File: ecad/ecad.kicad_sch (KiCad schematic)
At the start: 28 parts, among them J1 Raspberry_Pi_2_3, Q1 BC547, Q2 BC547, Q4 BC547, SW1 Power Button, SW2 SW_Push, SW3 SW_Push, U2 USB PD/QC Decoy, U3 VRB1205YMD_6wr3, U6 Power Bank

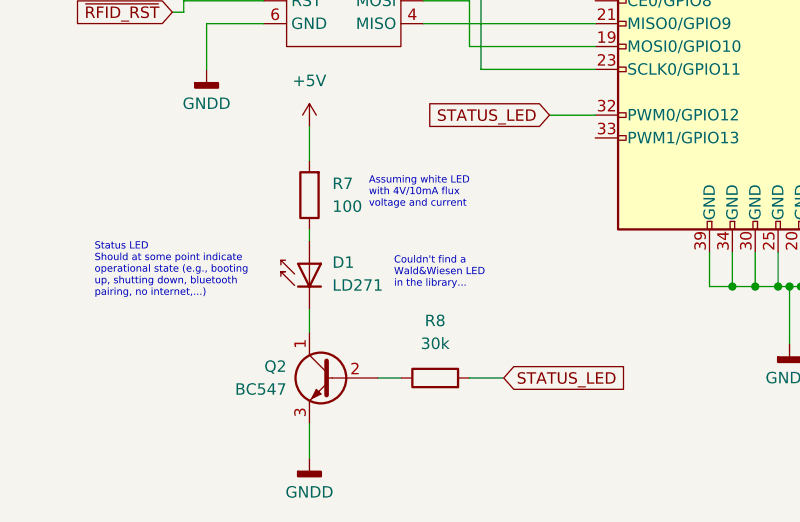
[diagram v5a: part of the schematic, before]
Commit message: Changed LED library element.
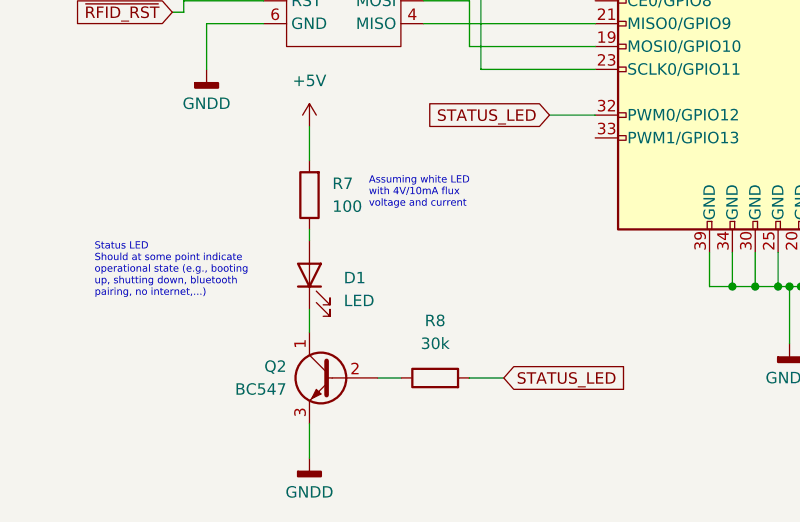
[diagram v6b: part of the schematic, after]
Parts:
- removed D1: LD271, LED_THT:LED_D5.0mm_IRGrey, symbol LED:LD271
- added D1: LED, symbol Device:LED
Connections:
- net at Q2.1 (C): now also D1.1 (K)
- net at R7.1: now also D1.2 (A)
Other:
- note removed: "Couldn't find a Wald&Wiesen LED in the library..."
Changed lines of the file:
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@@
 		)
 	)
-	(text "Couldn't find a\nWald&Wiesen LED\nin the library..."
-		(exclude_from_sim no)
-		(at 51.308 171.704 0)
-		(effects
-			(font
-				(size 0.8 0.8)
-			)
-			(justify left bottom)
-		)
-	)
 	(text "We need some clarification which grounds\nare connected on the amp board"
 		(exclude_from_sim no)
@@
 	)
 	(symbol
-		(lib_id "LED:LD271")
-		(at 41.91 168.91 90)
-		(unit 1)
-		(exclude_from_sim no)
-		(in_bom yes)
-		(on_board yes)
-		(dnp no)
-		(fields_autoplaced yes)
-		(property "Reference" "D1"
-			(at 44.45 168.7829 90)
-			(effects
-				(font
-					(size 1.27 1.27)
-				)
-				(justify right)
-			)
-		)
-		(property "Value" "LD271"
-			(at 44.45 171.3229 90)
-			(effects
-				(font
-					(size 1.27 1.27)
-				)
-				(justify right)
-			)
-		)
-		(property "Footprint" "LED_THT:LED_D5.0mm_IRGrey"
-			(at 37.465 168.91 0)
-			(effects
-				(font
-					(size 1.27 1.27)
-				)
-				(hide yes)
-			)
-		)
-		(property "Datasheet" "http://www.alliedelec.com/m/d/40788c34903a719969df15f1fbea1056.pdf"
-			(at 41.91 170.18 0)
-			(effects
-				(font
-					(size 1.27 1.27)
-				)
-				(hide yes)
-			)
-		)
-		(property "Description" "940nm IR-LED, 5mm"
-			(at 41.91 168.91 0)
-			(effects
-				(font
-					(size 1.27 1.27)
-				)
-				(hide yes)
-			)
-		)
-		(pin "2"
-		)
-		(pin "1"
-		)
-		(instances
-			(project ""
-				(path "/860b7f0e-7c1a-48cf-84ab-a41a24b3371c"
-					(reference "D1")
-					(unit 1)
-				)
-			)
-		)
-	)
-	(symbol
 		(lib_id "power:VPP")
 		(at 49.53 58.42 0)
@@
 					(unit 1)
 				)
+			)
+		)
+	)
+	(symbol
+		(lib_id "Device:LED")
+		(at 41.91 170.18 90)
+		(unit 1)
+		(exclude_from_sim no)
+		(in_bom yes)
+		(on_board yes)
+		(dnp no)
+		(fields_autoplaced yes)
+		(property "Reference" "D1"
+			(at 45.72 170.4974 90)
+			(effects
+				(font
+					(size 1.27 1.27)
+				)
+				(justify right)
+			)
+		)
+		(property "Value" "LED"
+			(at 45.72 173.0374 90)
+			(effects
+				(font
+					(size 1.27 1.27)
+				)
+				(justify right)
+			)
+		)
+		(property "Footprint" ""
+			(at 41.91 170.18 0)
+			(effects
+				(font
+					(size 1.27 1.27)
+				)
+				(hide yes)
+			)
+		)
+		(property "Datasheet" "~"
+			(at 41.91 170.18 0)
+			(effects
+				(font
+					(size 1.27 1.27)
+				)
+				(hide yes)
+			)
+		)
+		(property "Description" "Light emitting diode"
+			(at 41.91 170.18 0)
+			(effects
+				(font
+					(size 1.27 1.27)
+				)
+				(hide yes)
+			)
+		)
+		(pin "1"
+		)
+		(pin "2"
+		)
+		(instances
+			(project ""
+				(path "/860b7f0e-7c1a-48cf-84ab-a41a24b3371c"
+					(reference "D1")
+					(unit 1)
+				)

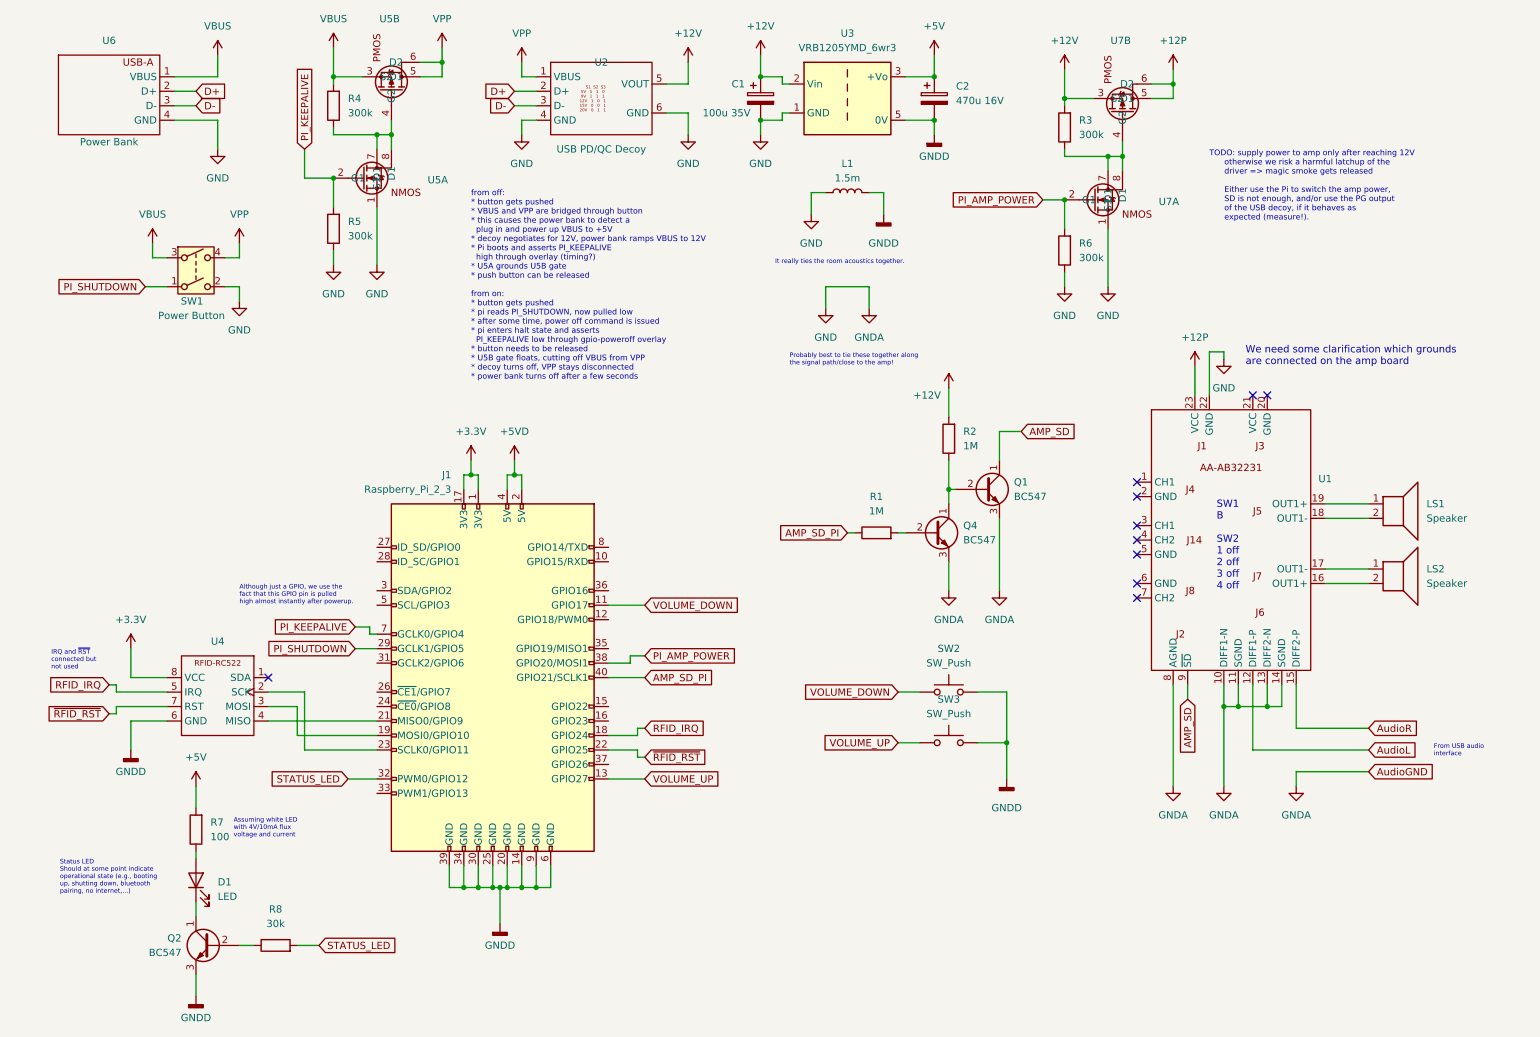
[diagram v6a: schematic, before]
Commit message: Replaced wrong +5V supply elements with +5VD
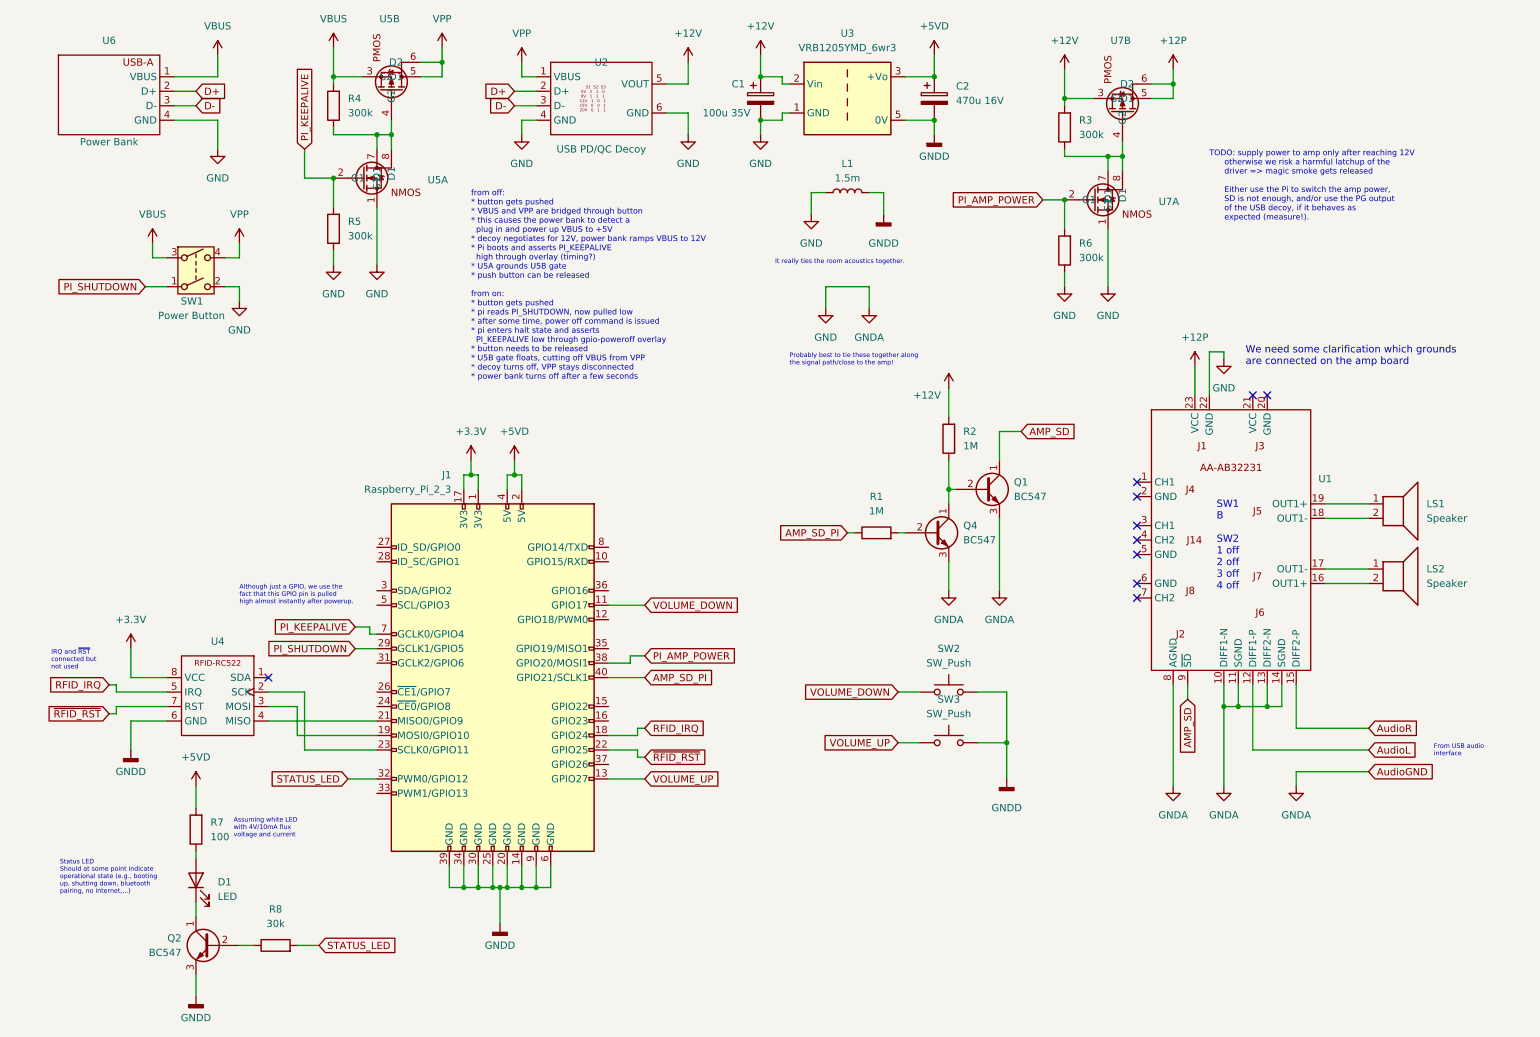
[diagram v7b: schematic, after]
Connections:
- net +5V is gone; now on net +5VD: C2.1, R7.2, U3.3 (+Vo)
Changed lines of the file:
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@@
+	)
+	(symbol
+		(lib_id "power:+5VD")
+		(at 41.91 153.67 0)
+		(unit 1)
+		(exclude_from_sim no)
+		(in_bom yes)
+		(on_board yes)
+		(dnp no)
+		(fields_autoplaced yes)
+		(property "Reference" "#PWR042"
+			(at 41.91 157.48 0)
+			(effects
+				(font
+					(size 1.27 1.27)
+				)
+				(hide yes)
+			)
+		)
+		(property "Value" "+5VD"
+			(at 41.91 148.59 0)
+			(effects
+				(font
+					(size 1.27 1.27)
+				)
+			)
+		)
+		(property "Footprint" ""
+			(at 41.91 153.67 0)
+			(effects
+				(font
+					(size 1.27 1.27)
+				)
+				(hide yes)
+			)
+		)
+		(property "Datasheet" ""
+			(at 41.91 153.67 0)
+			(effects
+				(font
+					(size 1.27 1.27)
+				)
+				(hide yes)
+			)
+		)
+		(property "Description" ""
+			(at 41.91 153.67 0)
+			(effects
+				(font
+					(size 1.27 1.27)
+				)
+				(hide yes)
+			)
+		)
+		(pin "1"
+		)
+		(instances
+			(project "ecad"
+				(path "/860b7f0e-7c1a-48cf-84ab-a41a24b3371c"
+					(reference "#PWR042")
+					(unit 1)
+				)
+			)
+		)
 	)
 	(symbol
@@
 				(path "/860b7f0e-7c1a-48cf-84ab-a41a24b3371c"
 					(reference "Q1")
-					(unit 1)
-				)
-			)
-		)
-	)
-	(symbol
-		(lib_id "power:+5V")
-		(at 41.91 153.67 0)
-		(unit 1)
-		(exclude_from_sim no)
-		(in_bom yes)
-		(on_board yes)
-		(dnp no)
-		(fields_autoplaced yes)
-		(property "Reference" "#PWR041"
-			(at 41.91 157.48 0)
-			(effects
-				(font
-					(size 1.27 1.27)
-				)
-				(hide yes)
-			)
-		)
-		(property "Value" "+5V"
-			(at 41.91 148.59 0)
-			(effects
-				(font
-					(size 1.27 1.27)
-				)
-			)
-		)
-		(property "Footprint" ""
-			(at 41.91 153.67 0)
-			(effects
-				(font
-					(size 1.27 1.27)
-				)
-				(hide yes)
-			)
-		)
-		(property "Datasheet" ""
-			(at 41.91 153.67 0)
-			(effects
-				(font
-					(size 1.27 1.27)
-				)
-				(hide yes)
-			)
-		)
-		(property "Description" ""
-			(at 41.91 153.67 0)
-			(effects
-				(font
-					(size 1.27 1.27)
-				)
-				(hide yes)
-			)
-		)
-		(pin "1"
-		)
-		(instances
-			(project "ecad"
-				(path "/860b7f0e-7c1a-48cf-84ab-a41a24b3371c"
-					(reference "#PWR041")
 					(unit 1)
 				)
@@
 	)
 	(symbol
+		(lib_id "power:+5VD")
+		(at 171.45 25.4 0)
+		(unit 1)
+		(exclude_from_sim no)
+		(in_bom yes)
+		(on_board yes)
+		(dnp no)
+		(fields_autoplaced yes)
+		(property "Reference" "#PWR016"
+			(at 171.45 29.21 0)
+			(effects
+				(font
+					(size 1.27 1.27)
+				)
+				(hide yes)
+			)
+		)
+		(property "Value" "+5VD"
+			(at 171.45 20.32 0)
+			(effects
+				(font
+					(size 1.27 1.27)
+				)
+			)
+		)
+		(property "Footprint" ""
+			(at 171.45 25.4 0)
+			(effects
+				(font
+					(size 1.27 1.27)
+				)
+				(hide yes)
+			)
+		)
+		(property "Datasheet" ""
+			(at 171.45 25.4 0)
+			(effects
+				(font
+					(size 1.27 1.27)
+				)
+				(hide yes)
+			)
+		)
+		(property "Description" ""
+			(at 171.45 25.4 0)
+			(effects
+				(font
+					(size 1.27 1.27)
+				)
+				(hide yes)
+			)
+		)
+		(pin "1"
+		)
+		(instances
+			(project "ecad"
+				(path "/860b7f0e-7c1a-48cf-84ab-a41a24b3371c"
+					(reference "#PWR016")
+					(unit 1)
+				)
+			)
+		)
+	)
+	(symbol
 		(lib_id "Switch:SW_Push")
 		(at 173.99 137.16 0)
@@
 					(unit 1)
 				)
-			)
-		)
-	)
-	(symbol
-		(lib_id "power:+5V")
-		(at 171.45 25.4 0)
-		(unit 1)
-		(exclude_from_sim no)
-		(in_bom yes)
-		(on_board yes)
-		(dnp no)
-		(fields_autoplaced yes)
-		(property "Reference" "#PWR016"
-			(at 171.45 29.21 0)
-			(effects
-				(font
-					(size 1.27 1.27)
-				)
-				(hide yes)
-			)
-		)
-		(property "Value" "+5V"
-			(at 171.45 20.32 0)
-			(effects
-				(font
-					(size 1.27 1.27)
-				)
-			)
-		)
-		(property "Footprint" ""
-			(at 171.45 25.4 0)
-			(effects
-				(font
-					(size 1.27 1.27)
-				)
-				(hide yes)
-			)
-		)
-		(property "Datasheet" ""
-			(at 171.45 25.4 0)
-			(effects
-				(font
-					(size 1.27 1.27)
-				)
-				(hide yes)
-			)
-		)
-		(property "Description" ""
-			(at 171.45 25.4 0)
-			(effects
-				(font
-					(size 1.27 1.27)
-				)
-				(hide yes)
-			)
-		)
-		(pin "1"
-		)
-		(instances
-			(project "ecad"
-				(path "/860b7f0e-7c1a-48cf-84ab-a41a24b3371c"
-					(reference "#PWR016")
-					(unit 1)
-				)
